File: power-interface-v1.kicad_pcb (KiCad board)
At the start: 2 copper layers, 56.5 x 49.8 mm, 14 parts, among them P1 PINBALL-CONNECTOR, P10 CONN_01X01, P2 PINBALL-CONNECTOR, P3 PINBALL-CONNECTOR, P4 PINBALL-CONNECTOR, P5 CONN_01X01, P6 CONN_01X01, P7 CONN_01X01, P8 CONN_01X01, P9 CONN_01X01

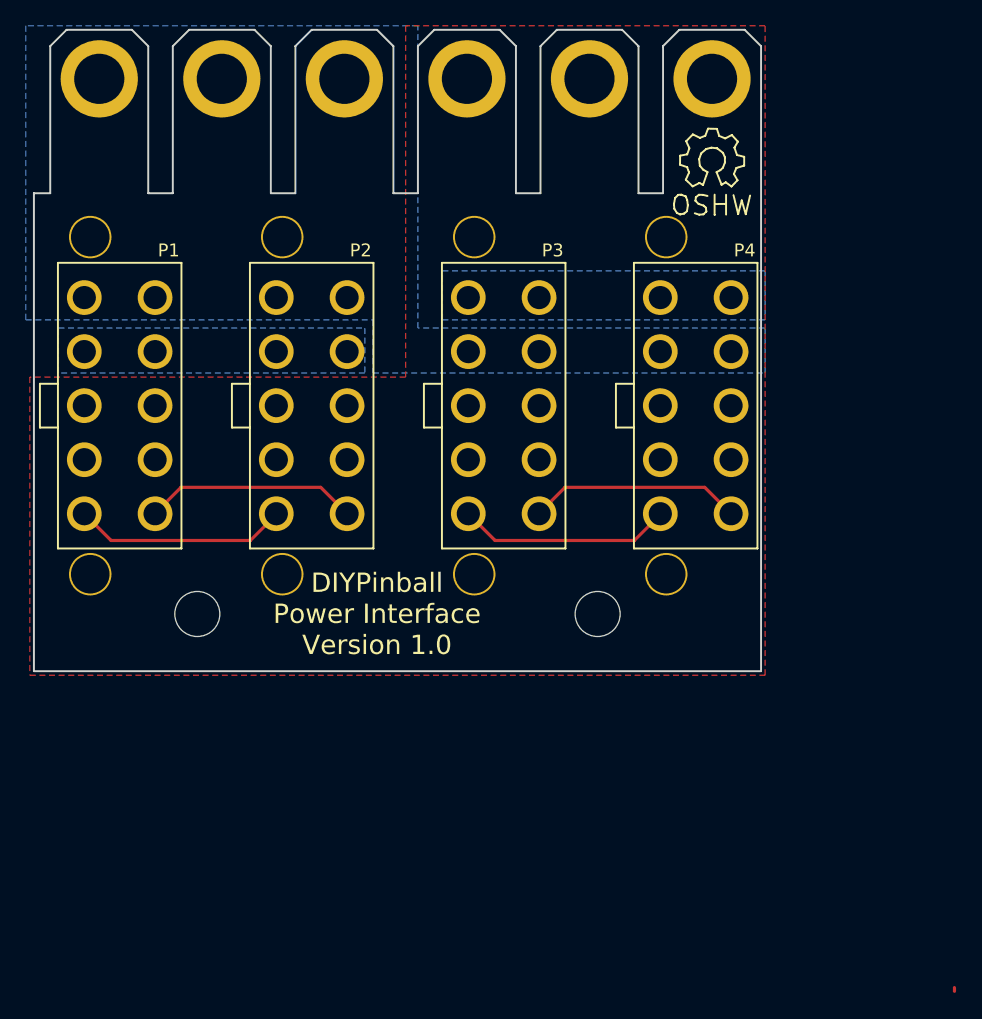
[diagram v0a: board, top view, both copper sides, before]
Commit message: Updating power interface to use fuses, and to use them to choose between a 12V and Vsol supply
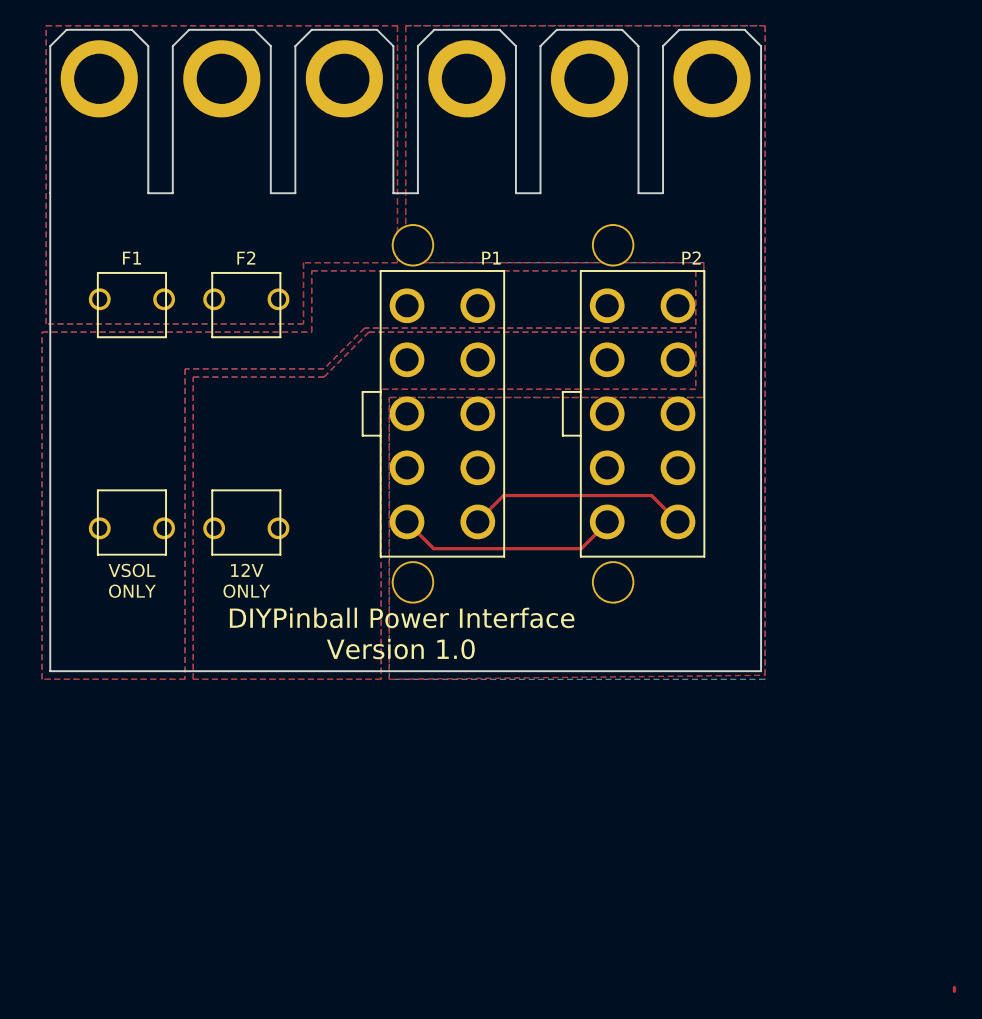
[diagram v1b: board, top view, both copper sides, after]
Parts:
- removed G***: DIYPINBALL-LOGO-SMALL, Pinball:diypinball-logo-small
- removed P10, P9: CONN_01X01, Pinball:PSU-HOLE
- removed REF** (x2): MountingHole_3-5mm, Mounting_Holes:MountingHole_3-5mm
- removed REF**: Symbol_OSHW-Logo_SilkScreen, Symbols:Symbol_OSHW-Logo_SilkScreen
- added F1: FUSE, Pinball:FC203-20MM, F.Cu at (126.0, 108.3)
- added F2: FUSE, Pinball:FC203-20MM, F.Cu at (134.9, 108.3)
- P3, P4: value PINBALL-CONNECTOR -> CONN_01X01; footprint Pinball:PINBALL-CONNECTOR-V -> Pinball:PSU-HOLE
- moved P4 44.7 mm to (133.0, 82.2), turned to 0 degrees
- moved P3 40.4 mm to (123.5, 82.2), turned to 0 degrees
- moved P2 25.7 mm to (165.7, 108.3)
- moved P1 25.1 mm to (150.2, 108.3)
- moved P5 19.1 mm to (142.6, 82.2)
- moved P6 19.1 mm to (152.1, 82.2)
- moved P7 19.0 mm to (161.6, 82.2)
- moved P8 19.0 mm to (171.1, 82.2)
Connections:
- P1 pad 1: /VOLTAGE_IN -> Net-(F1-Pad1)
- P1 pad 6: /VOLTAGE_IN -> Net-(F1-Pad1)
- P2 pad 1: /VOLTAGE_IN -> Net-(F1-Pad1)
- P2 pad 6: /VOLTAGE_IN -> Net-(F1-Pad1)
- P3 pad 1: Net-(P3-Pad1) -> Net-(F1-Pad2)
- P4 pad 1: Net-(P3-Pad1) -> Net-(F1-Pad2)
- P5 pad 1: /VOLTAGE_IN -> Net-(F1-Pad2)
- P6 pad 1: /VOLTAGE_IN -> GND
- P7 pad 1: /VOLTAGE_IN -> GND
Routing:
- net Net-(P3-Pad10): track 16.7 -> 0.00 mm
- net Net-(P3-Pad5): track 16.6 -> 0.00 mm
- net Net-(P1-Pad5): track 16.6 -> 17.3 mm
- net Net-(P1-Pad10): track 16.7 -> 17.3 mm
- added copper zone on B.Cu, net GND
- added copper zone on B.Cu, net Net-(F1-Pad1)
- added copper zone on F.Cu, net Net-(F1-Pad1)
- added copper zone on B.Cu, net Net-(F1-Pad2)
- added copper zone on F.Cu, net Net-(F1-Pad2)
- added copper zone on F.Cu, net Net-(F2-Pad1)
- removed copper zone on B.Cu, net /VOLTAGE_IN
- removed copper zone on B.Cu, net Net-(P3-Pad1)
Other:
- board size 56.5 x 49.8 mm -> 55.2 x 49.8 mm
- board text added: "12V ONLY"
- board text added: "VSOL ONLY"
- board text removed: "P1 and P2 for Vsol"
- board text removed: "P3 and P4 for 12V"
